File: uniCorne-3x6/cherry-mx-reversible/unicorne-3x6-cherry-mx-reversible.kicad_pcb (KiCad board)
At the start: 2 copper layers, 133.8 x 91.4 mm, 98 parts, among them J1 MJ-4PP-9, J2 Nice!View, J3 Conn_01x02, J4 Conn_01x03, SW1 SW_MX_HS, SW10 SW_MX_HS, SW11 SW_MX_HS, SW12 SW_MX_HS, SW13 SW_MX_HS, SW14 SW_MX_HS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

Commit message: uniCorne 3x6 chocolate
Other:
- board text added: "uniCorne Cherry 3x6"
- board text removed: "uniCorne Cherry"

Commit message: small tweak
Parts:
- U1: footprint TB2086_MISC:ProMicro-ish-dn-rev-unrouted_3x5 -> TB2086_MISC:ProMicro-ish-dn-rev-unrouted_3x6
- moved R3 1.13 mm to (184.5, 110.1)
- moved R4 1.13 mm to (184.5, 112.1)
- moved JP9 0.76 mm to (188.6, 111.0)
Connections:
- PSW1 pad 1: unconnected-(PSW1-A-Pad1) -> BAT+
- PSW1 pad 3: BAT+ -> unconnected-(PSW1-C-Pad3)
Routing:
- net unconnected-(U1-RAW-Pad24): track 28.3 -> 10.9 mm
- net LED: track 65.3 -> 82.3 mm, vias 2 -> 3
- net DATA: track 64.8 -> 76.3 mm
- net unconnected-(PSW1-A-Pad1): track 6.23 -> 0.00 mm
- net unconnected-(PSW1-C-Pad3): track 0.00 -> 5.32 mm
- net BAT+: track 17.4 -> 14.0 mm
- net SDA: track 72.5 -> 69.1 mm
- net GND: track 34.8 -> 38.2 mm, vias 14 -> 15
- net RESET: track 58.8 -> 62.1 mm
- net row3: track 117.9 -> 114.9 mm
- net row0: track 158.6 -> 161.2 mm, vias 1 -> 2
- net col3: track 171.3 -> 168.9 mm
- net SCL: track 60.3 -> 58.6 mm
- net row2: track 153.0 -> 154.6 mm, vias 1 -> 2
- net col1: track 174.2 -> 172.7 mm
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
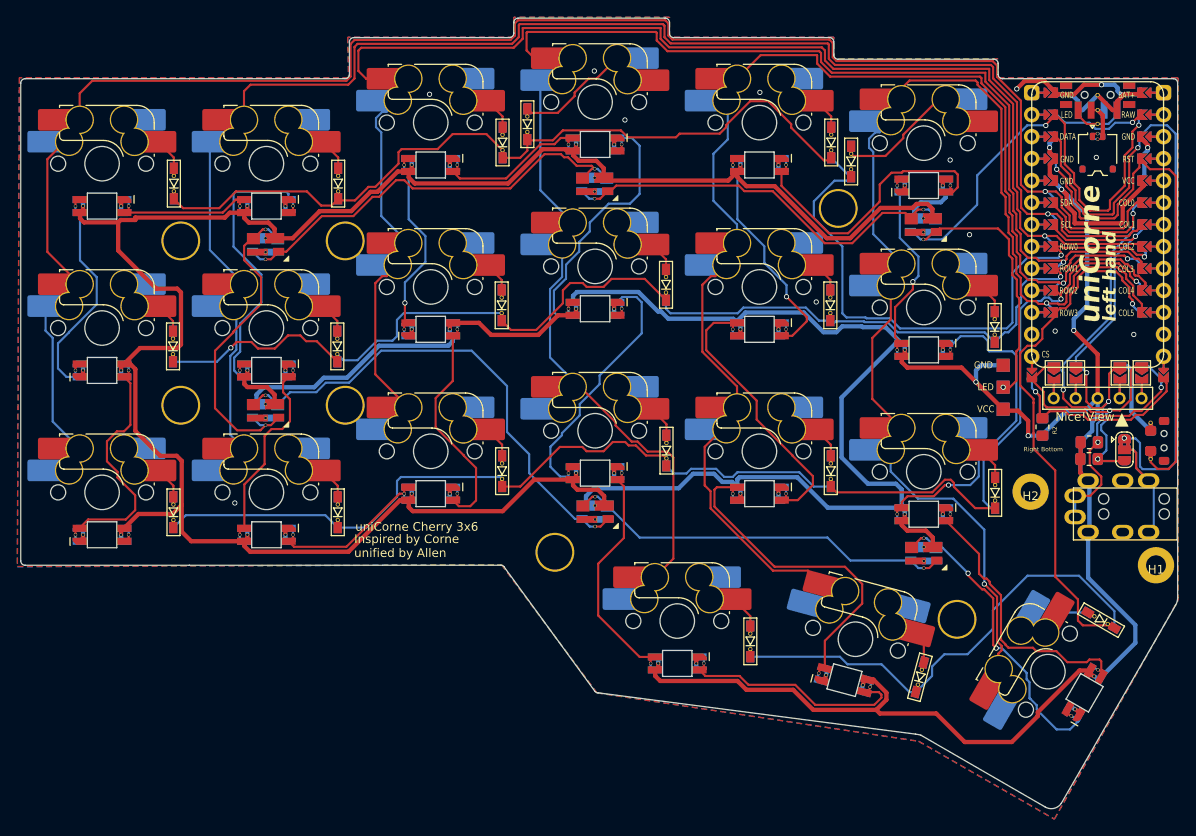
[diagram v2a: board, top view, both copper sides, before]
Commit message: amended footprint for LED
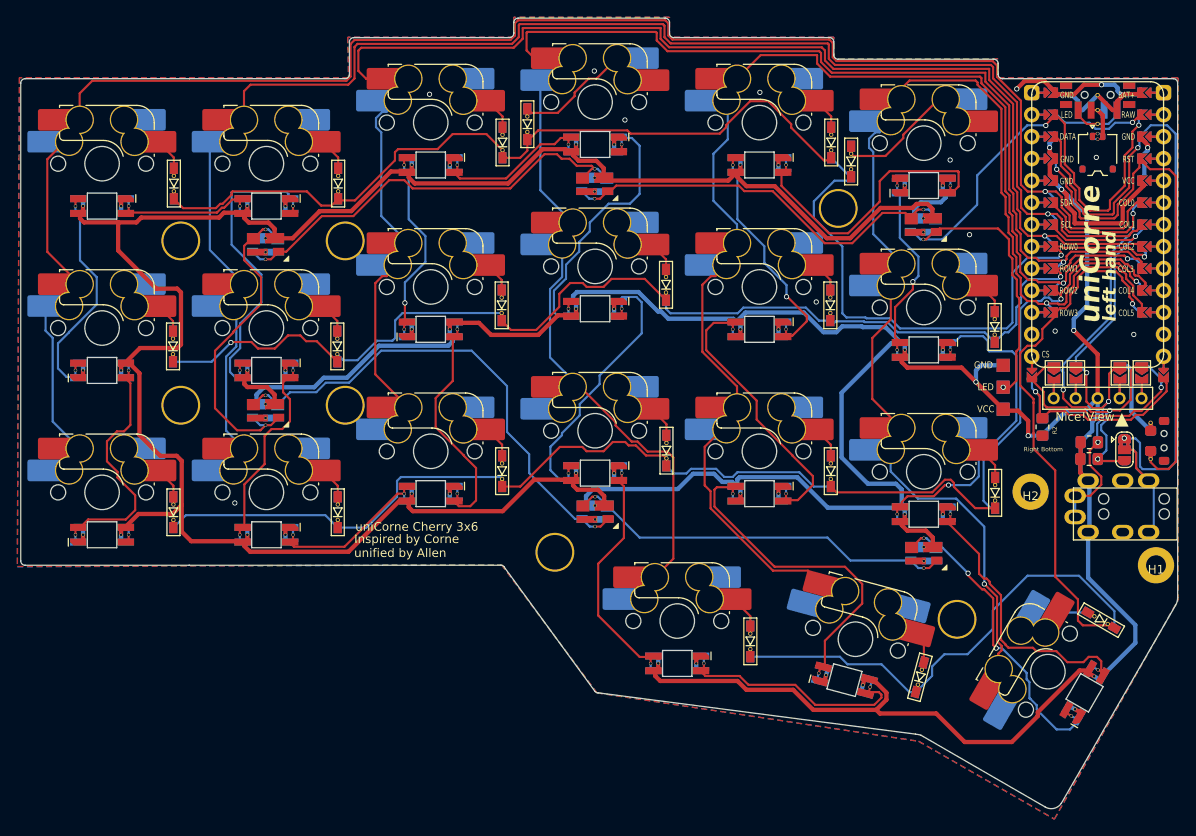
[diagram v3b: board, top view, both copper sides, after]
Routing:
- net VCC: track 588.2 -> 586.1 mm
- net Net-(L2-DIN): track 31.3 -> 32.5 mm
- net Net-(L21-DIN): track 35.1 -> 34.5 mm

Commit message: small tweak
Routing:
- net VCC: track 586.1 -> 587.7 mm
- net Net-(L12-DIN): track 36.2 -> 37.2 mm
- net row2: track 154.6 -> 153.9 mm
- net Net-(L16-DIN): track 25.8 -> 26.4 mm

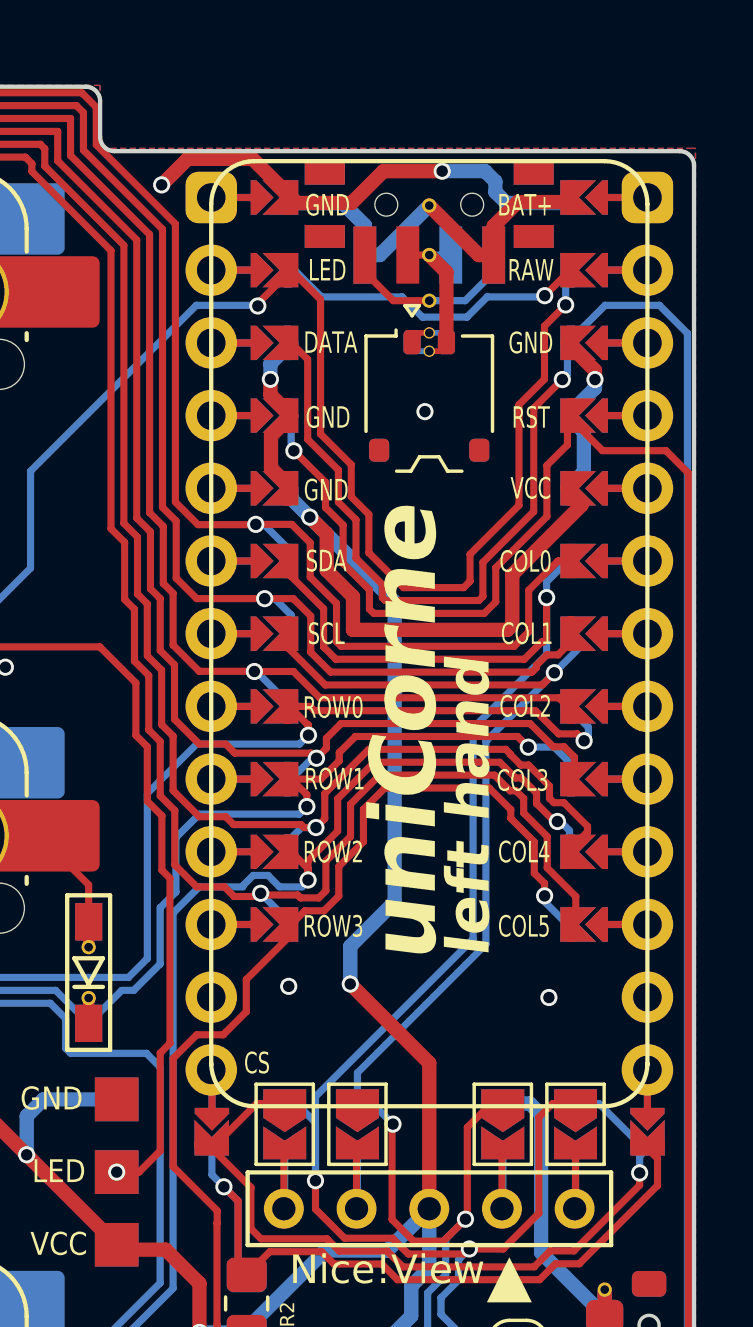
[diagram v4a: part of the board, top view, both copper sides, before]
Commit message: fixed footprint for promicro-ish 3x6
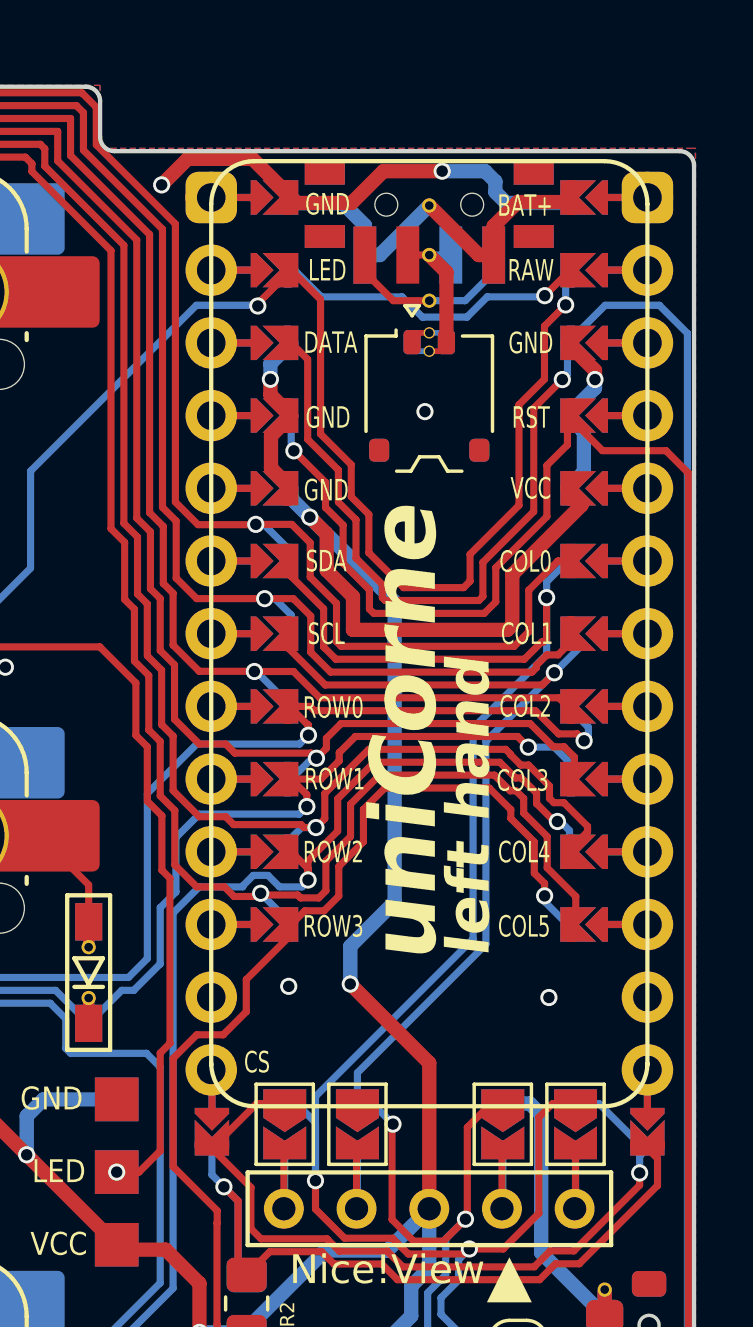
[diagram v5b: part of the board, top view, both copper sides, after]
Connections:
- U1 pad 12: IS_LEFT -> CS
- U1 pad 13: CS -> IS_LEFT
